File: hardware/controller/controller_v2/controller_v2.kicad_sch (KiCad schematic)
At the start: 22 parts, among them J1 USB_C_Receptacle_USB2.0_16P, J2 Conn_01x04_Socket, SW1 SW_Push, SW2 SW_Push, U1 ESP32-C3-MINI-1-N4, U2 74AHCT1G125, U4 AMS1117-3.3

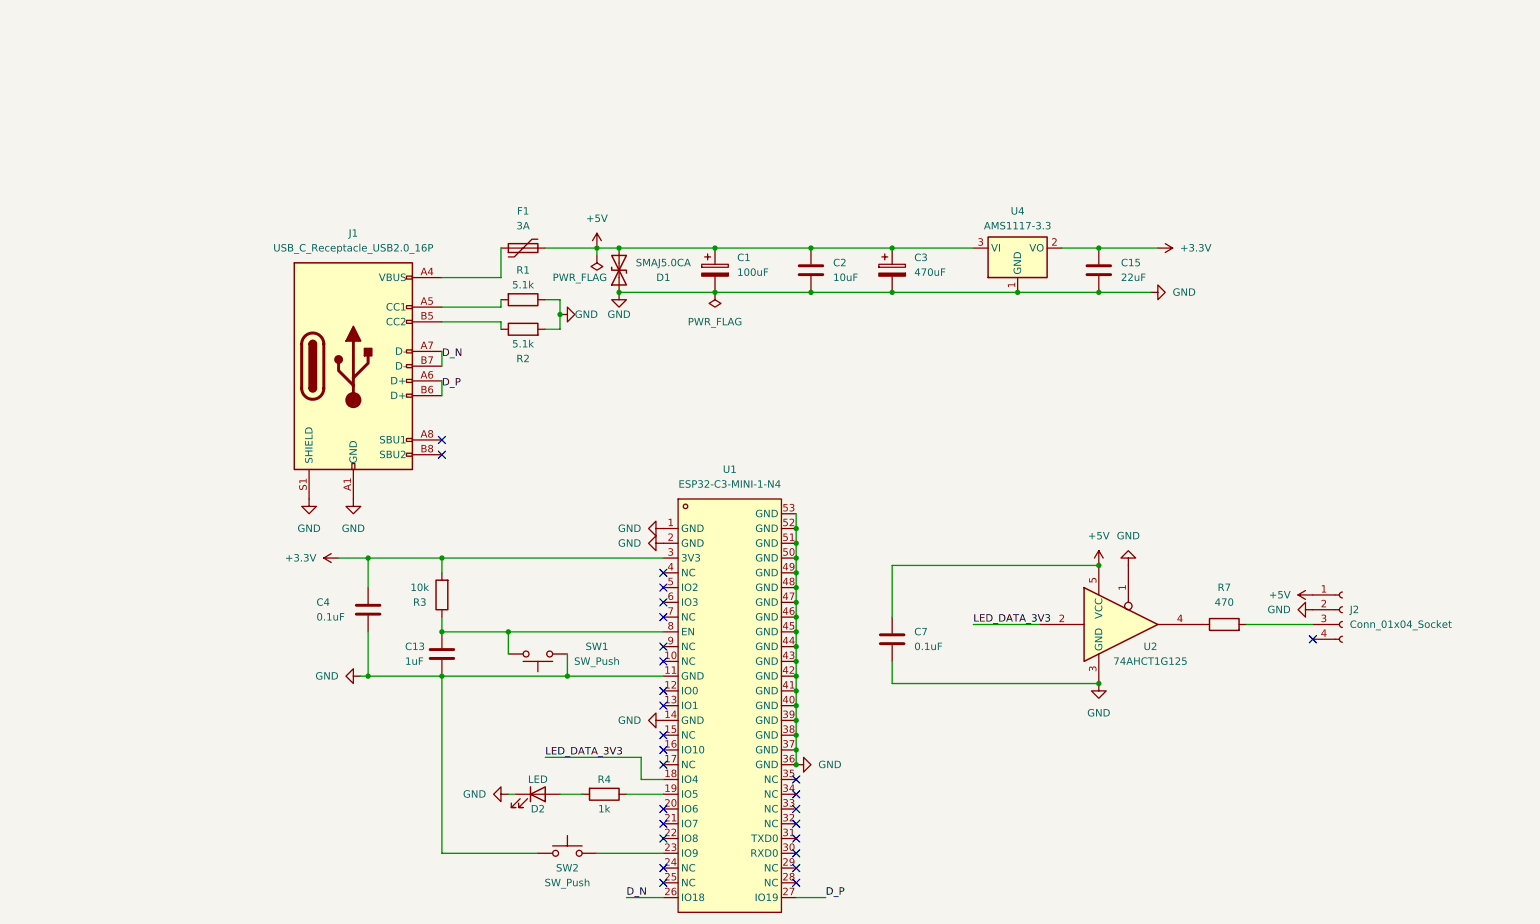
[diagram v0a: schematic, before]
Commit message: Add octave-module flex PCB (fab-ready) + hardware to main
octave-module: uniform 13.708 mm LED pitch (caps aligned), solder lap-seam (J2 output / J3 input pads) with J2 plated 0.8 mm solder-access holes, full routing + GND pour, J1 placement; seam-lap footprint library; spacing/seam design docs; regenerated BOM + production files (J1 DNP, caps C14663, LEDs C2761795). Also controller_v2 + hardware BOM/docs.

Co-Authored-By: Claude Opus 4.8 <noreply@anthropic.com>
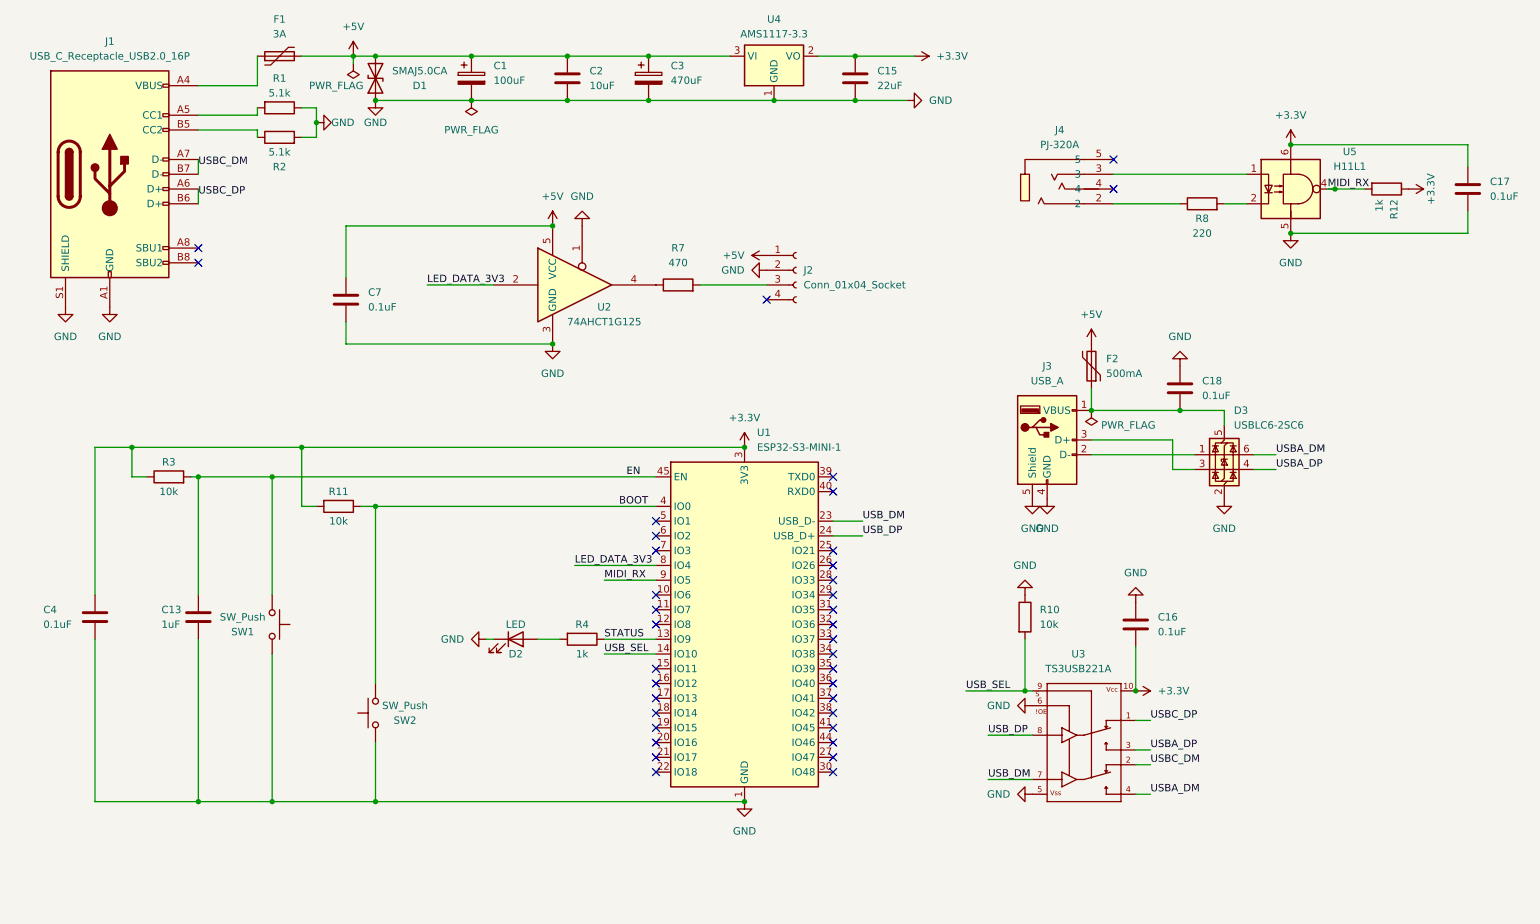
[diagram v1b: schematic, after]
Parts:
- removed U1: ESP32-C3-MINI-1-N4, ESP32-C3-MINI-1:WIFIM-SMD_ESP32-C3-MINI-1, symbol ESP32-C3-MINI-1:ESP32-C3-MINI-1-N4
- added C16, C17, C18: 0.1uF, Capacitor_SMD:C_0603_1608Metric, symbol Device:C
- added D3: USBLC6-2SC6, Package_TO_SOT_SMD:SOT-23-6, symbol Power_Protection:USBLC6-2SC6
- added F2: 500mA, Fuse:Fuse_1206_3216Metric, symbol Device:Polyfuse
- added J3: USB_A, easyeda2kicad:USB-A-TH__USB-AF-90, symbol Connector:USB_A
- added J4: PJ-320A, easyeda2kicad:AUDIO-TH_XKB_PJ-320A, symbol easyeda2kicad:PJ-320A
- added R10, R11: 10k, Resistor_SMD:R_0603_1608Metric, symbol Device:R
- added R12: 1k, Resistor_SMD:R_0603_1608Metric, symbol Device:R
- added R8: 220, Resistor_SMD:R_0603_1608Metric, symbol Device:R
- added U1: ESP32-S3-MINI-1, RF_Module:ESP32-S2-MINI-1, symbol RF_Module:ESP32-S3-MINI-1
- added U3: TS3USB221A, TS3USB221A:QFN-10-RSE, symbol TS3USB221A:TS3USB221A
- added U5: H11L1, H11L1SM:IC_H11L1SM, symbol Isolator:H11L1
- SW1, SW2: footprint Button_Switch_SMD:SW_SPST_PTS645Sx43SMTR92 -> easyeda2kicad:SW-SMD_4P-L5.1-W5.1-P3.70-LS6.5-TL_H1.5
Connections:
- net +3.3V: now also R3.1, C16.2, C17.2, R11.2, R12.1, U1.3 (3V3), U3.10, U5.6; no longer R3.2
- net +5V: now also F2.2
- net GND: now also SW1.2, C16.1, C17.1, C18.2, D3.2 (GND), J3.4 (GND), J3.5 (Shield), R10.1, U1.1 (GND), U1.2 (GND), U1.42 (GND), U1.43 (GND), U1.46 (GND), U1.47 (GND), U1.48 (GND), U1.49 (GND), U1.50 (GND), U1.51 (GND), U1.52 (GND), U1.53 (GND), U1.54 (GND), U1.55 (GND), U1.56 (GND), U1.57 (GND), U1.58 (GND), U1.59 (GND), U1.60 (GND), U1.61 (GND), U1.62 (GND), U1.63 (GND), U1.64 (GND), U1.65 (GND), U3.5, U3.6, U5.5; no longer SW1.1
- net LED_DATA_3V3: now also U1.8 (IO4)
- net STATUS: now reaches R4.1
- net STATUS: now also U1.13 (IO9)
- net BOOT: now reaches SW2.2
- net BOOT: now also R11.1, U1.4 (IO0)
- net D_N renamed USBC_DM
- net USBC_DM: now also U3.2
- net D_P renamed USBC_DP
- net USBC_DP: now also U3.1
- new net: C18.1, D3.5 (VBUS), F2.1, J3.1 (VBUS)
- new net: D3.1 (I/O1), J3.2 (D-)
- new net: D3.3 (I/O2), J3.3 (D+)
- new net: J4.2, R8.1
- new net: J4.3, U5.1
- new net: R8.2, U5.2
- new net EN: C13.1, R3.2, SW1.1, U1.45 (EN)
- new net MIDI_RX: R12.2, U1.9 (IO5), U5.4
- new net USBA_DM: D3.6 (I/O1), U3.4
- new net USBA_DP: D3.4 (I/O2), U3.3
- new net USB_DM: U1.23 (USB_D-), U3.7
- new net USB_DP: U1.24 (USB_D+), U3.8
- new net USB_SEL: R10.2, U1.14 (IO10), U3.9
- no-connect marks 27 -> 37
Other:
- moved on the sheet: C1, C13, C15, C2, C3, C4, C7, D1, D2, F1, J1, J2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
